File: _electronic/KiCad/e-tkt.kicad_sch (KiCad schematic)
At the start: 64 parts, among them J2 USB4120-03-C_REVA, Q1 SS8050-G, Q2 SS8050-G, U2 AZ1117I-3.3, U6 ESP32-S3-WROOM-1-N8R2

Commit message: improved pcb design, with parts in stock
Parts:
- removed C14, C15: 47pF, Capacitor_SMD:C_0603_1608Metric_Pad1.08x0.95mm_HandSolder, symbol Device:C
- removed C17: 100nF, Capacitor_SMD:C_0603_1608Metric_Pad1.08x0.95mm_HandSolder, symbol Device:C
- removed C18: 4.7uF, Capacitor_Tantalum_SMD:CP_EIA-1608-10_AVX-L_Pad1.25x1.05mm_HandSolder, symbol Device:C_Polarized
- removed D_RX1, D_TX1: LED, LED_SMD:LED_0805_2012Metric, symbol Device:LED
- removed FB1: FerriteBead, Inductor_SMD:L_0603_1608Metric_Pad1.05x0.95mm_HandSolder, symbol Device:FerriteBead
- removed R19, R20: 27R, Resistor_SMD:R_0603_1608Metric_Pad0.98x0.95mm_HandSolder, symbol Device:R
- removed R2, R3: 470R, Resistor_SMD:R_0603_1608Metric_Pad0.98x0.95mm_HandSolder, symbol Device:R
- added D1, D10, D4, D9, D_USBIN1: LED, LED_SMD:LED_0603_1608Metric_Pad1.05x0.95mm_HandSolder, symbol Device:LED
- added D3: BAT760,115, Diode_SMD:D_SOD-323, symbol Diode:BAT41
- added JP1, JP2, JP3: SolderJumper_2_Bridged, Jumper:SolderJumper-2_P1.3mm_Bridged2Bar_Pad1.0x1.5mm, symbol Jumper:SolderJumper_2_Bridged
- added R5: 10K(5%), Resistor_SMD:R_0603_1608Metric, symbol Device:R
- added R6: 100R, Resistor_SMD:R_0603_1608Metric_Pad0.98x0.95mm_HandSolder, symbol Device:R
- added TP_12v1, TP_3.3v1, TP_5v1, TP_6v1, TP_CTS1, TP_DTR1, TP_GND1, TP_GND2, TP_GND3, TP_RX1, TP_TX1, TP_VCC_3.3V1: TestPoint, TestPoint:TestPoint_Pad_D1.0mm, symbol Connector:TestPoint
- C1, C3, C4, C7: Id (none) -> CGA3E2X7R1H104K080AA
- C10: Id (none) -> C1608X5R1E106M080AC
- C11, C6: Id (none) -> C1608JB1A226M080AC
- C12: footprint Capacitor_Tantalum_SMD:CP_EIA-1608-10_AVX-L_Pad1.25x1.05mm_HandSolder -> Capacitor_Tantalum_SMD:CP_EIA-3216-10_Kemet-I_Pad1.58x1.35mm_HandSolder
- C13: value 10nF -> 10uF/25v; Id (none) -> C1608X5R1E106M080AC
- C8: value 10uF -> 100uF; footprint Capacitor_Tantalum_SMD:CP_EIA-1608-10_AVX-L_Pad1.25x1.05mm_HandSolder -> Capacitor_SMD:CP_Elec_6.3x5.9; Id (none) -> 16TZV100M6.3X6.1
- C9: footprint Capacitor_Tantalum_SMD:CP_EIA-1608-10_AVX-L_Pad1.25x1.05mm_HandSolder -> Capacitor_Tantalum_SMD:CP_EIA-3216-10_Kemet-I_Pad1.58x1.35mm_HandSolder; Id (none) -> TAJA106K016RNJ
- D2: footprint LED_SMD:LED_0805_2012Metric -> LED_SMD:LED_0603_1608Metric_Pad1.05x0.95mm_HandSolder; Id (none) -> B1931TW--20P000314U1930
- F2: Id (none) -> B59606A0110A062
- J2: Id (none) -> USB4120-03-C
- J_masterpower1: Id (none) -> DCJ200-10-A-K1-K
- Q1, Q2: Id (none) -> SS8050-G
- Q_HALL1, Q_SERVO1: Id (none) -> BSS138W-TP
- R1, R10, R11, R12, R13, R7, R8: Id (none) -> ERJ-3EKF1002V
- R15, R16, R17, R18: value 470 -> 430R; Id (none) -> ERJ-PA3F4300V
- R21, R22: Id (none) -> ERJ-3EKF5101V
- R4: value 10K -> 10K(5%); Id (none) -> ERJ-3EKF1002V
- S_BOOT1, S_RESET1, S_WIFIRESET1: Id (none) -> TS06-667-25-BK-100-G-SMT-TR
- S_power1: Id (none) -> JS202011JCQN
- U2: Id (none) -> AZ1117IH-3.3TRG1
- U6: Id (none) -> ESP32-S3-WROOM-1-N8R2
- U_6v2: Id (none) -> L7806ABD2T-TR
- U_DRIVER1: Id (none) -> ULN2003ADR2G
- renumbered J_NEMA1 to J_17HS4023_1, J_STEPPER1 to J_28byj-48-12v_1, J_LED_FINISH1 to J_LED_END1, J_LED_CAROUSEL1 to J_LED_PRESS1
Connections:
- net IO19 is gone; now on net IO19 D-: U6.13 (IO19)
- net IO20 is gone; now on net IO20 D+: U6.14 (IO20)
- net VIN is gone; now on net +12V: C10.1, S_power1.3, U2.3 (IN)
- net +12V: now also TP_12v1.1
- net +3.3V: now also R1.2, R4.2, JP1.1 (A), JP2.1 (A), JP3.1 (A), R5.1, TP_3.3v1.1, TP_VCC_3.3V1.1; no longer A_DRIVER1.10 (MS1), A_DRIVER1.11 (MS2), A_DRIVER1.12 (MS3), R1.1, R4.1
- net +5V: now also C13.2, D3.1 (K), R6.1, TP_5v1.1; no longer F2.2
- net +6V: now also TP_6v1.1
- net EN: now also R1.1, S_BOOT1.2, TP_DTR1.1; no longer C1.1, R1.2, S_BOOT1.3
- net GNDREF: now also C1.1, S_BOOT1.3, S_RESET1.3, S_WIFIRESET1.3, D_USBIN1.1 (K), TP_GND1.1, TP_GND2.1, TP_GND3.1; no longer C1.2, S_BOOT1.2, S_RESET1.2, S_WIFIRESET1.2
- net IO0: no longer C3.2, S_RESET1.3, S_RESET1.4, U6.27 (IO0)
- net IO10: now also U_DRIVER1.4 (I4); no longer Q_SERVO1.2 (S), R13.1
- net IO11: now also U_DRIVER1.3 (I3); no longer U_DRIVER1.4 (I4)
- net IO12: now also U_DRIVER1.2 (I2); no longer U_DRIVER1.3 (I3)
- net IO13: now also U_DRIVER1.1 (I1); no longer U_DRIVER1.2 (I2)
- net IO14: now also J_OLED1.4 (Pin_4); no longer U_DRIVER1.1 (I1)
- net IO16: now also J_LED_END1.2 (Pin_2)
- net IO17: now also J_LED_PRESS1.2 (Pin_2)
- net IO21: now also J_OLED1.3 (Pin_3)
- net IO38: now also C1.2, R4.1, S_WIFIRESET1.2, S_WIFIRESET1.4; no longer J_LED_END1.2 (Pin_2)
- net IO45: now also D1.2 (A); no longer A_DRIVER1.16 (DIR)
- net IO46: now also D9.1 (K)
- net IO47: now also A_DRIVER1.16 (DIR); no longer J_OLED1.4 (Pin_4)
- net IO48: now also D4.2 (A); no longer J_OLED1.3 (Pin_3)
- net IO20 D+: now reaches J2.A6 (D1+), J2.B6 (D2+)
- net at J2.A4 (VBUS_A), J2.A9 (VBUS_A), J2.B4 (VBUS_B)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: now also F2.1; no longer C13.2
- net RXD0: now reaches U6.36 (RXD0)
- net RXD0: now also TP_TX1.1
- net TXD0: now reaches U6.37 (TXD0)
- net TXD0: now also TP_RX1.1
- net IO19 D-: now reaches J2.A7 (D1-), J2.B7 (D2-)
- net IO1: no longer names the net of U6.39 (IO1)
- net IO15: no longer names the net of U6.8 (IO15)
- net IO18: no longer names the net of U6.11 (IO18)
- net IO2: no longer names the net of U6.38 (IO2)
- net IO3: no longer names the net of U6.15 (IO3)
- net IO35: no longer names the net of U6.28 (IO35)
- net IO35: no longer A_DRIVER1.9 (~{ENABLE})
- net IO36: no longer names the net of U6.29 (IO36)
- net IO36: no longer A_DRIVER1.15 (STEP)
- net IO37: no longer names the net of U6.30 (IO37)
- net IO37: no longer J_LED_PRESS1.2 (Pin_2)
- removed net IO39: R4.2, S_WIFIRESET1.3, S_WIFIRESET1.4, U6.32 (IO39)
- net IO4: no longer names the net of U6.4 (IO4)
- net IO40: no longer names the net of U6.33 (IO40)
- net IO41: no longer names the net of U6.34 (IO41)
- net IO42: no longer names the net of U6.35 (IO42)
- net IO5: no longer names the net of U6.5 (IO5)
- net IO6: no longer names the net of U6.6 (IO6)
- net IO7: no longer names the net of U6.7 (IO7)
- net IO8: no longer names the net of U6.12 (IO8)
- net IO9: no longer names the net of Q_HALL1.2 (S), R11.1
- net IO9: now also D9.2 (A); no longer U6.17 (IO9)
- new net: D_USBIN1.2 (A), R6.2
- new net: D3.2 (A), F2.2
- new net: D10.1 (K), Q_SERVO1.2 (S), R13.1
- new net: A_DRIVER1.10 (MS1), JP1.2 (B)
- new net: A_DRIVER1.15 (STEP), D1.1 (K)
- new net: A_DRIVER1.9 (~{ENABLE}), D4.1 (K)
- new net: A_DRIVER1.11 (MS2), JP2.2 (B)
- new net: A_DRIVER1.12 (MS3), JP3.2 (B)
- new net IO0 RESET: C3.2, R5.2, S_RESET1.2, S_RESET1.4, TP_CTS1.1, U6.27 (IO0)
- new net IO09: D10.2 (A), U6.17 (IO9)
- no-connect marks 13 -> 28
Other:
- note added: "12V POWER"
- note added: "EXTERNAL FLASHING"
- note added: "TESTING"
- note added: "USB-C (2.0)"
- note removed: "5v on barrel pin 3?"
- note removed: "9-12V EXTERNAL POWER"
- note removed: "DIODE?"
- note removed: "LED voltage resistors values (5-12v?)"
- note removed: "USB-C (2.0) / UART"
- note removed: "reatribute pins (from ESP32 to ESP32-S3)"
- moved on the sheet: A_DRIVER1, C10, C11, C12, C13, C3, C4, C6, C7, C8, C9, D2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

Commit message: needs revision
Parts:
- removed D2: LED, LED_SMD:LED_0603_1608Metric_Pad1.05x0.95mm_HandSolder, symbol Device:LED
- added D11: LED, LED_SMD:LED_0603_1608Metric_Pad1.05x0.95mm_HandSolder, symbol Device:LED
- added R2: 430R, Resistor_SMD:R_0603_1608Metric, symbol Device:R
- added TP_IO15, TP_IO18, TP_IO5, TP_IO6, TP_IO7, TP_IO8: TestPoint, TestPoint:TestPoint_Pad_D1.0mm, symbol Connector:TestPoint
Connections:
- net +12V: now also R2.1
- net +3.3V: now also C11.1
- net GNDREF: now also D11.1 (K)
- net at U6.11 (IO18): now also TP_IO18.1
- net at U6.12 (IO8): now also TP_IO8.1
- net at U6.5 (IO5): now also TP_IO5.1
- net at U6.6 (IO6): now also TP_IO6.1
- net at U6.7 (IO7): now also TP_IO7.1
- net at U6.8 (IO15): now also TP_IO15.1
- new net: D11.2 (A), R2.2
- no-connect marks 28 -> 22
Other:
- moved on the sheet: C10, C11, S_power1

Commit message: tvs diode, ground plane, schematics layout
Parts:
- removed C13: 10uF/25v, Capacitor_SMD:C_0603_1608Metric_Pad1.08x0.95mm_HandSolder, symbol Device:C
- removed F2: 500mA, Fuse:Fuse_1210_3225Metric_Pad1.42x2.65mm_HandSolder, symbol Device:Polyfuse
- added C2: 10uF/25v, Capacitor_SMD:C_0603_1608Metric_Pad1.08x0.95mm_HandSolder, symbol Device:C
- added H1, H2: MountingHole_Pad, MountingHole:MountingHole_3.2mm_M3, symbol Mechanical:MountingHole_Pad
- added H3, H4: MountingHole_Pad, MountingHole:MountingHole_3.2mm_M3_Pad_Via, symbol Mechanical:MountingHole_Pad
- added U1: USB6B1, Package_SO:SOIC-8_3.9x4.9mm_P1.27mm, symbol Power_Protection:USB6B1
- U6: footprint SnapEDA Library:XCVR_ESP32-S3-WROOM-1-N16R2 -> RF_Module:ESP32-S3-WROOM-1
- U_6v2: footprint Package_TO_SOT_SMD:TO-263-3_TabPin2 -> Package_TO_SOT_SMD:TO-263-2
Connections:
- net +5V: now also R6.2, C2.2; no longer R6.1
- net GNDREF: now also C2.1, H1.1, H2.1, H3.1, H4.1, U1.4 (GND), U1.5 (GND)
- net IO19 D-: now also U1.7 (I/O1); no longer J2.A7 (D1-), J2.B7 (D2-)
- net IO20 D+: now also U1.6 (I/O2); no longer J2.A6 (D1+), J2.B6 (D2+)
- net at D_USBIN1.2 (A): now also R6.1; no longer R6.2
- net VBUS_A: now reaches D3.2 (A)
- net VBUS_A: now also J2.A4 (VBUS_A), J2.A9 (VBUS_A), J2.B4 (VBUS_B), J2.B9 (VBUS_B), U1.1 (VBUS), U1.8 (VBUS)
- new net D1+: J2.A6 (D1+), J2.B6 (D2+), U1.3 (I/O2)
- new net D1-: J2.A7 (D1-), J2.B7 (D2-), U1.2 (I/O1)
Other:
- moved on the sheet: A_DRIVER1, C1, C10, C11, C12, C3, C4, C6, C7, C8, C9, D1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

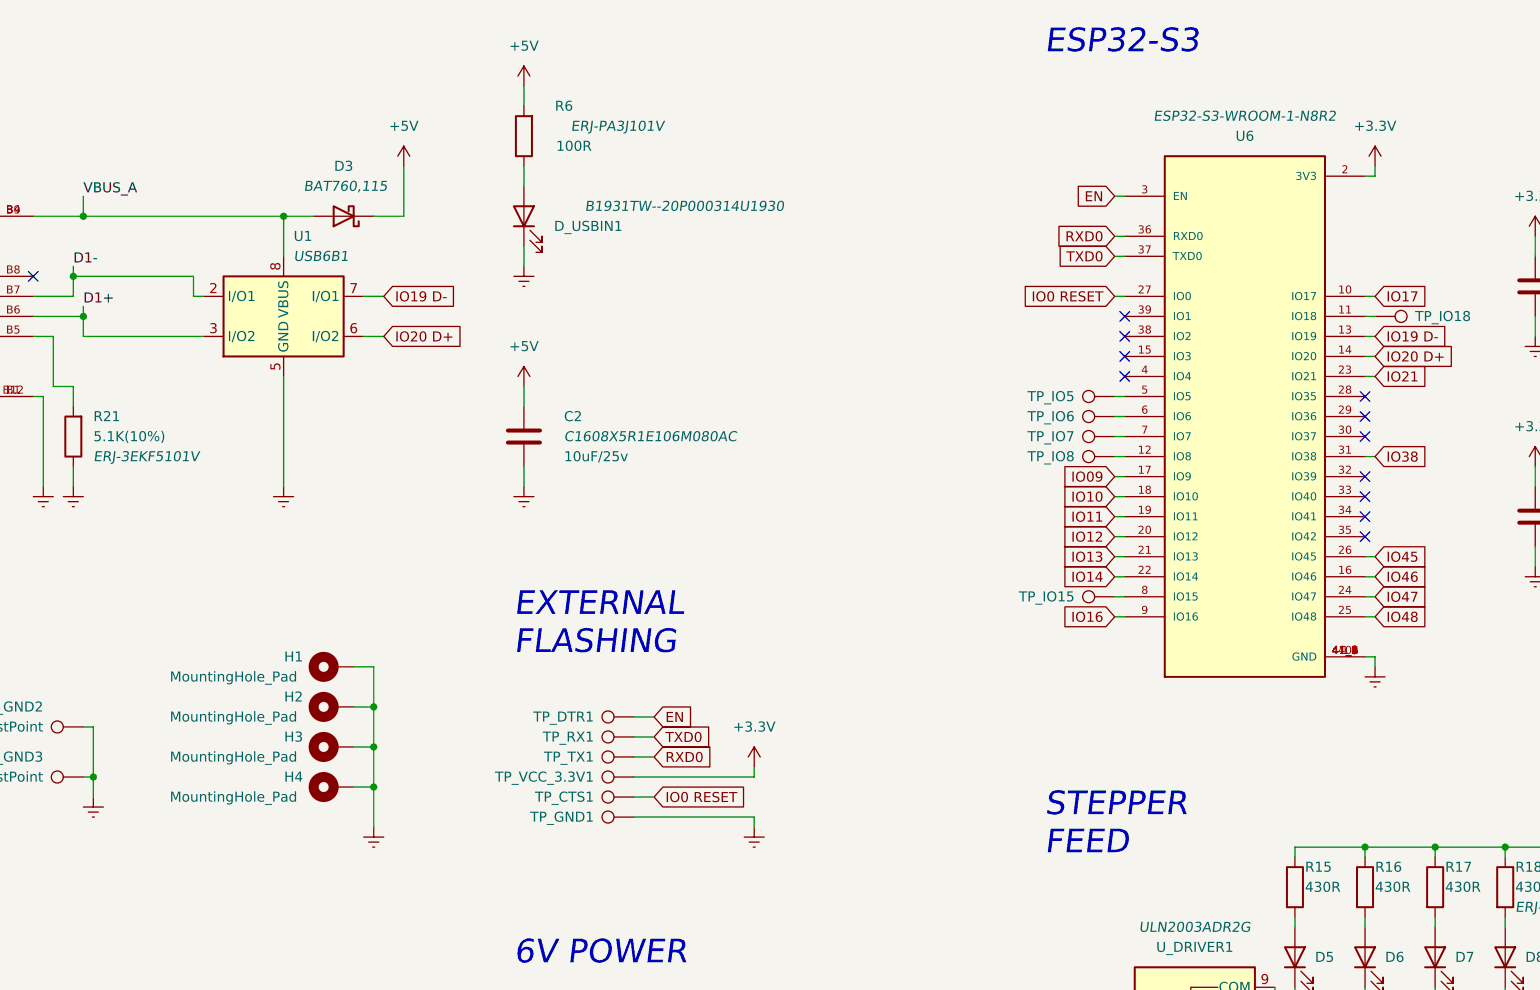
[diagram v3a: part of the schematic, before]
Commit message: fixed esp footprint/symbol, plus vias and holes
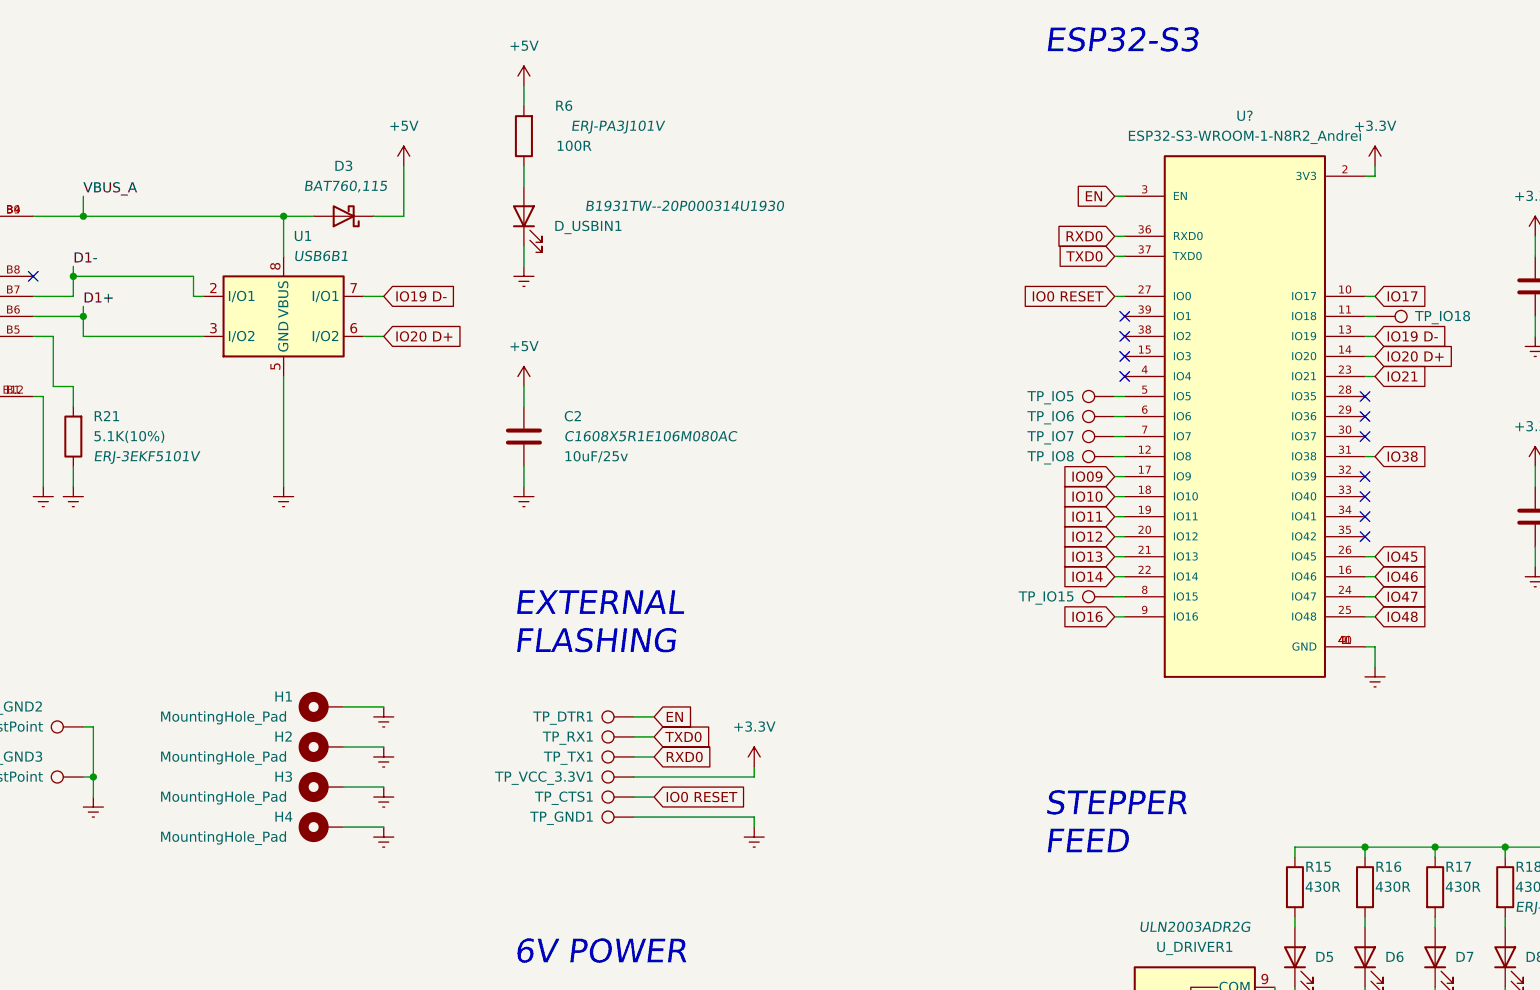
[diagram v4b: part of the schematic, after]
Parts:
- removed U6: ESP32-S3-WROOM-1-N8R2, RF_Module:ESP32-S3-WROOM-1, symbol ESP32-S3-WROOM-1-N16R2:ESP32-S3-WROOM-1-N16R2
- added U?: ESP32-S3-WROOM-1-N8R2_Andrei, SnapEDA Library:ESP32-S3-WROOM-1_Andrei, symbol ESP32-S3-WROOM-1-N16R2:ESP32-S3-WROOM-1-N8R2_Andrei
- H1, H2: footprint MountingHole:MountingHole_3.2mm_M3 -> MountingHole:MountingHole_3.2mm_M3_Pad_Via
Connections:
- net +3.3V: now also U?.2 (3V3)
- net EN: now also U?.3 (EN)
- net GNDREF: now also U?.1 (GND), U?.40 (GND), U?.41 (GND)
- net IO0 RESET: now also U?.27 (IO0)
- net IO09: now also U?.17 (IO9)
- net IO10: now also U?.18 (IO10)
- net IO11: now also U?.19 (IO11)
- net IO12: now also U?.20 (IO12)
- net IO13: now also U?.21 (IO13)
- net IO14: now also U?.22 (IO14)
- net IO16: now also U?.9 (IO16)
- net IO17: now also U?.10 (IO17)
- net IO19 D-: now also U?.13 (IO19)
- net IO20 D+: now also U?.14 (IO20)
- net IO21: now also U?.23 (IO21)
- net IO38: now also U?.31 (IO38)
- net IO45: now also U?.26 (IO45)
- net IO46: now also U?.16 (IO46)
- net IO47: now also U?.24 (IO47)
- net IO48: now also U?.25 (IO48)
- net RXD0: now also U?.36 (RXD0)
- net TXD0: now also U?.37 (TXD0)
- net at TP_IO6.1: now also U?.6 (IO6)
- net at TP_IO18.1: now also U?.11 (IO18)
- net at TP_IO8.1: now also U?.12 (IO8)
- net at TP_IO5.1: now also U?.5 (IO5)
- net at TP_IO7.1: now also U?.7 (IO7)
- net at TP_IO15.1: now also U?.8 (IO15)
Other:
- moved on the sheet: H3, H4

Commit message: bigger board, switch back to esp32
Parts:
- removed D3: BAT760,115, Diode_SMD:D_SOD-323, symbol Diode:BAT41
- removed J2: USB4120-03-C_REVA, SnapEDA Library:GCT_USB4120-03-C_REVA, symbol USB4120-03-C_REVA:USB4120-03-C_REVA
- removed R21, R22: 5.1K(10%), Resistor_SMD:R_0603_1608Metric_Pad0.98x0.95mm_HandSolder, symbol Device:R
- removed S_power1: JS202011JCQN, SnapEDA Library:SW_JS202011JCQN, symbol JS202011JCQN:JS202011JCQN
- removed U?: ESP32-S3-WROOM-1-N8R2_Andrei, SnapEDA Library:ESP32-S3-WROOM-1_Andrei, symbol ESP32-S3-WROOM-1-N16R2:ESP32-S3-WROOM-1-N8R2_Andrei
- added D2: BAT760,115, Diode_SMD:D_SOD-323, symbol Diode:BAT41
- added H5, H6: MountingHole_Pad, MountingHole:MountingHole_3.2mm_M3_Pad_Via, symbol Mechanical:MountingHole_Pad
- added J1: USB4105-GF-A, SnapEDA Library:GCT_USB4105-GF-A, symbol USB4105-GF-A:USB4105-GF-A
- added J_USBPOWER1: Conn_01x02_Male, Connector_PinHeader_2.54mm:PinHeader_1x02_P2.54mm_Vertical, symbol Connector:Conn_01x02_Male
- added R3, R9: 5.1K(10%), Resistor_SMD:R_0603_1608Metric_Pad0.98x0.95mm_HandSolder, symbol Device:R
- added U3: FT231XS, Package_SO:SSOP-20_3.9x8.7mm_P0.635mm, symbol Interface_USB:FT231XS
- added U4: ESP32-WROOM-32, RF_Module:ESP32-WROOM-32, symbol RF_Module:ESP32-WROOM-32
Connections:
- net IO0 is gone; now on net IO0 RESET: Q2.3 (C)
- net IO09 is gone; now on net IO14: D10.2 (A)
- net IO10 is gone; now on net IO16: U_DRIVER1.4 (I4)
- net IO38 is gone; now on net IO13: C1.2, R4.1, S_WIFIRESET1.2, S_WIFIRESET1.4
- net +12V: now also J_masterpower1.1, J_USBPOWER1.1 (Pin_1)
- net +3.3V: now also U4.2 (VDD)
- net +5V: now also D2.1 (K), J_USBPOWER1.2 (Pin_2)
- net D1+: now also U1.2 (I/O1), J1.A6 (DP1), J1.B6 (DP2); no longer U1.3 (I/O2)
- net D1-: now also U1.3 (I/O2), J1.A7 (DN1), J1.B7 (DN2); no longer U1.2 (I/O1)
- net EN: now also U4.3 (EN)
- net GNDREF: now also H5.1, H6.1, J1.A1_B12 (GND), J1.B1_A12 (GND), J1.S1 (SHELL_GND), J1.S2 (SHELL_GND), J1.S3 (SHELL_GND), J1.S4 (SHELL_GND), R3.1, R9.1, U3.6 (GND), U4.1 (GND), U4.15 (GND), U4.38 (GND), U4.39 (GND)
- net IO0 RESET: now also U4.25 (IO0)
- net IO12: now also U4.14 (IO12); no longer U_DRIVER1.2 (I2)
- net IO13: now also U4.16 (IO13); no longer U_DRIVER1.1 (I1)
- net IO14: now also U4.13 (IO14); no longer J_OLED1.4 (Pin_4)
- net IO16: now also U4.27 (IO16); no longer J_LED_END1.2 (Pin_2)
- net IO17: now also U4.28 (IO17)
- net IO21: now also J_OLED1.4 (Pin_4), U4.33 (IO21); no longer J_OLED1.3 (Pin_3)
- net at A_DRIVER1.3 (1B): now also J_17HS4023_1.4 (Pin_4); no longer J_17HS4023_1.1 (Pin_1)
- net at A_DRIVER1.4 (1A): now also J_17HS4023_1.3 (Pin_3); no longer J_17HS4023_1.2 (Pin_2)
- net at A_DRIVER1.5 (2A): now also J_17HS4023_1.2 (Pin_2); no longer J_17HS4023_1.3 (Pin_3)
- net at A_DRIVER1.6 (2B): now also J_17HS4023_1.1 (Pin_1); no longer J_17HS4023_1.4 (Pin_4)
- net IO11 renamed IO2
- net IO2: now also U4.24 (IO2)
- net IO19 D- renamed D+
- net D+: now also U3.11 (USBDP)
- net IO20 D+ renamed D-
- net D-: now also U3.12 (USBDM)
- net IO45 renamed IO32
- net IO32: now also U4.8 (IO32)
- net IO46 renamed IO34
- net IO34: now also U4.6 (IO34)
- net IO47 renamed IO33
- net IO33: now also U4.9 (IO33)
- net IO48 renamed IO25
- net IO25: now also U4.10 (IO25)
- net RXD0 renamed RXD0 IO3
- net RXD0 IO3: now also U3.20 (TXD), U4.34 (RXD0/IO3)
- net TXD0 renamed TXD0 IO1
- net TXD0 IO1: now also U3.4 (RXD), U4.35 (TXD0/IO1)
- net VBUS_A: no longer names the net of U1.1 (VBUS), U1.8 (VBUS)
- net VBUS_A: now also D2.2 (A), J1.A4_B9 (VBUS), J1.B4_A9 (VBUS)
- new net: J1.A5 (CC1), R3.2
- new net: J1.B5 (CC2), R9.2
- new net IO15: U4.23 (IO15), U_DRIVER1.1 (I1)
- new net IO18: U4.30 (IO18)
- new net IO19: U4.31 (IO19)
- new net IO22: J_OLED1.3 (Pin_3), U4.36 (IO22)
- new net IO23: U4.37 (IO23)
- new net IO26: U4.11 (IO26)
- new net IO27: U4.12 (IO27)
- new net IO35: U4.7 (IO35)
- new net IO4: U4.26 (IO4), U_DRIVER1.2 (I2)
- new net IO5: J_LED_END1.2 (Pin_2), U4.29 (IO5)
- no-connect marks 22 -> 11
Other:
- note added: "ESP32"
- note removed: "ESP32-S3"
- moved on the sheet: A_DRIVER1, C1, C12, C2, C3, C4, C6, C7, C8, C9, D1, D4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
